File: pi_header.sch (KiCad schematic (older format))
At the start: 1 part

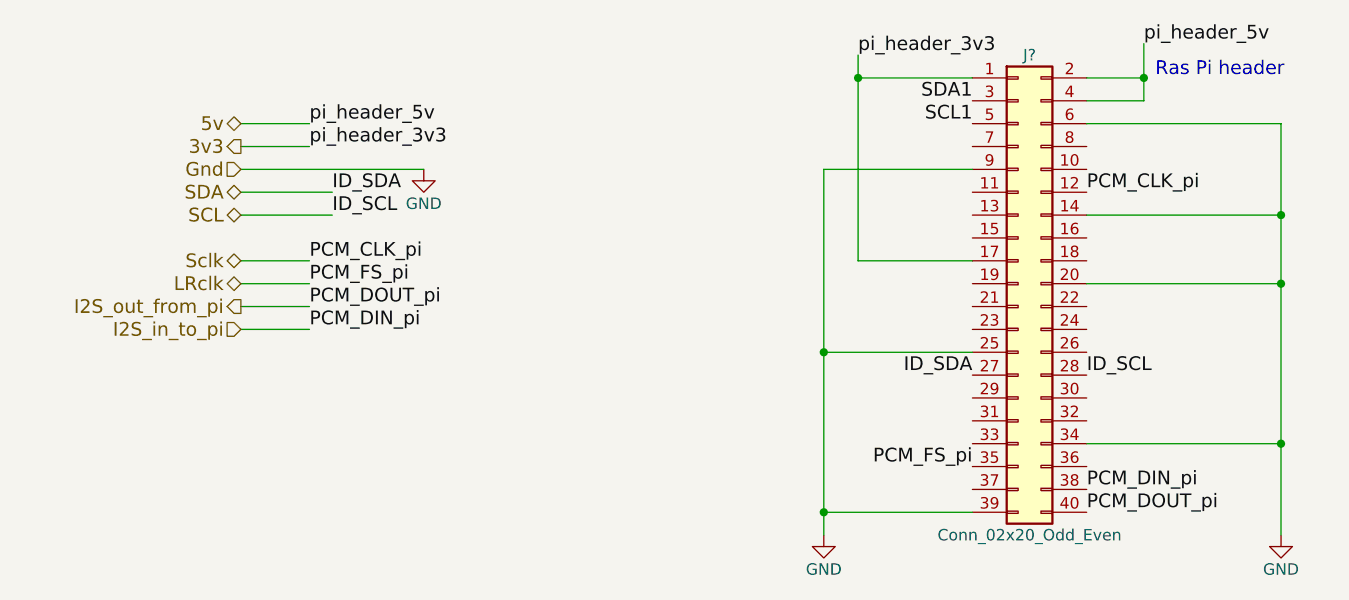
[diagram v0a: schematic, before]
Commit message: preliminary schematic using discrete logic chips
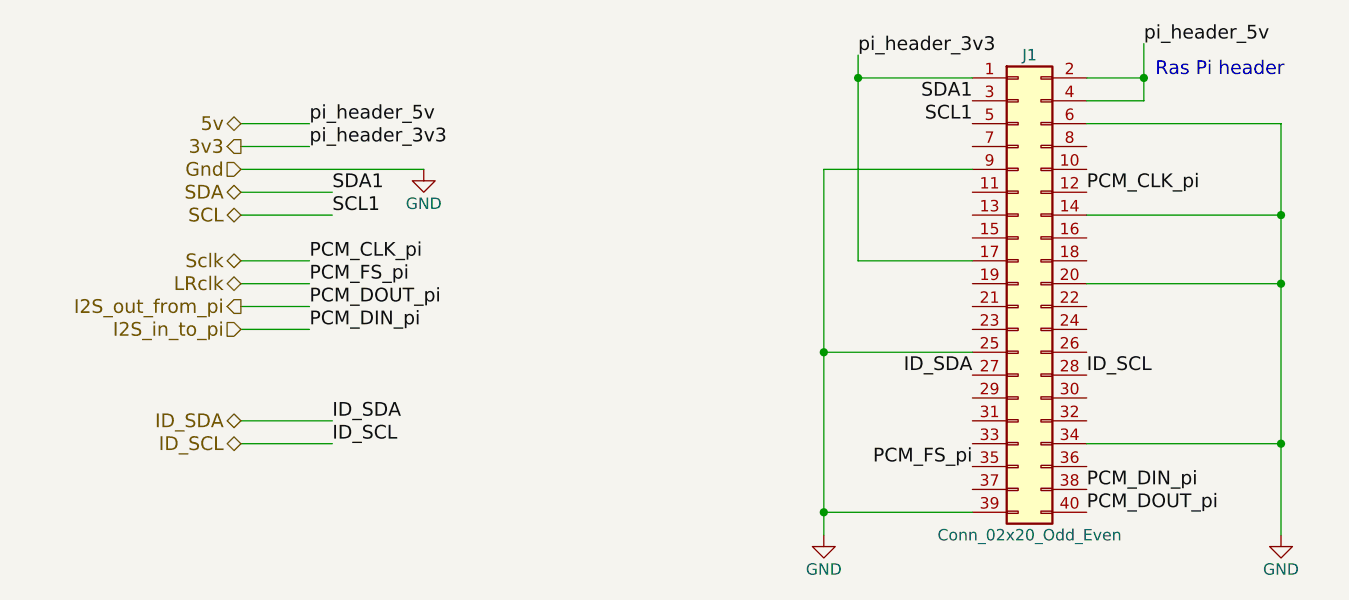
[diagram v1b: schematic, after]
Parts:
- J1: renamed from J?; footprint (none) -> Pin_Headers:Pin_Header_Straight_2x20_Pitch2.54mm
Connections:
- net SCL1 is gone; now on net SCL: J1.5 (Pin_5)
- net SDA1 is gone; now on net SDA: J1.3 (Pin_3)
- net SCL: no longer J1.28 (Pin_28)
- net SDA: no longer J1.27 (Pin_27)
- new net ID_SCL: J1.28 (Pin_28)
- new net ID_SDA: J1.27 (Pin_27)
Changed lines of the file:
@@
 LIBS:contrib
 LIBS:valves
+LIBS:74cbtlv3245
+LIBS:abb
+LIBS:tca9546a
 LIBS:flexibleaudiohub-cache
 EELAYER 25 0
@@
 $Descr A4 11693 8268
 encoding utf-8
-Sheet 2 9
+Sheet 2 10
 Title ""
 Date ""
@@
 Ras Pi header
 Wire Wire Line
-	4000 1800 4000 1900
-Wire Wire Line
-	4000 1900 4000 2700
+	4000 1800 4000 2700
 Wire Wire Line
 	4000 1900 4500 1900
@@
 Connection ~ 4000 1900
 $Comp
-L GND #PWR013
+L GND #PWR023
 U 1 1 58D8CF97
 P 3850 3900
-F 0 "#PWR013" H 3850 3650 50  0001 C CNN
+F 0 "#PWR023" H 3850 3650 50  0001 C CNN
 F 1 "GND" H 3850 3750 50  0000 C CNN
 F 2 "" H 3850 3900 50  0000 C CNN
@@
 	3850 3800 4500 3800
 Wire Wire Line
-	3850 2300 3850 3100
-Wire Wire Line
-	3850 3100 3850 3800
-Wire Wire Line
-	3850 3800 3850 3900
+	3850 2300 3850 3900
 Wire Wire Line
 	4500 3100 3850 3100
@@
 	5000 1900 5250 1900
 Wire Wire Line
-	5250 1750 5250 1900
-Wire Wire Line
-	5250 1900 5250 2000
+	5250 1750 5250 2000
 Wire Wire Line
 	5250 2000 5000 2000
 Connection ~ 5250 1900
 $Comp
-L GND #PWR015
+L GND #PWR024
 U 1 1 58D8CFAF
 P 5850 3900
-F 0 "#PWR015" H 5850 3650 50  0001 C CNN
+F 0 "#PWR024" H 5850 3650 50  0001 C CNN
 F 1 "GND" H 5850 3750 50  0000 C CNN
 F 2 "" H 5850 3900 50  0000 C CNN
@@
 	5850 3500 5000 3500
 Wire Wire Line
-	5850 2100 5850 2500
-Wire Wire Line
-	5850 2500 5850 2800
-Wire Wire Line
-	5850 2800 5850 3500
-Wire Wire Line
-	5850 3500 5850 3900
+	5850 2100 5850 3900
 Wire Wire Line
 	5000 2800 5850 2800
@@
 PCM_DOUT_pi
 $Comp
-L GND #PWR018
+L GND #PWR025
 U 1 1 58D8D147
 P 2100 2300
-F 0 "#PWR018" H 2100 2050 50  0001 C CNN
+F 0 "#PWR025" H 2100 2050 50  0001 C CNN
 F 1 "GND" H 2100 2150 50  0000 C CNN
 F 2 "" H 2100 2300 50  0000 C CNN
@@
 	1300 3000 1600 3000
 $Comp
-L Conn_02x20_Odd_Even J?
+L Conn_02x20_Odd_Even J1
 U 1 1 5AD71FB3
 P 4700 2800
-F 0 "J?" H 4750 3800 50  0000 C CNN
+F 0 "J1" H 4750 3800 50  0000 C CNN
 F 1 "Conn_02x20_Odd_Even" H 4750 1700 50  0000 C CNN
-F 2 "" H 4700 2800 50  0001 C CNN
+F 2 "Pin_Headers:Pin_Header_Straight_2x20_Pitch2.54mm" H 4700 2800 50  0001 C CNN
 F 3 "" H 4700 2800 50  0001 C CNN
 	1    4700 2800
@@
 $EndComp
 Text Label 1700 2400 0    60   ~ 0
-ID_SDA
+SDA1
 Text Label 1700 2500 0    60   ~ 0
-ID_SCL
+SCL1
 Text Label 4000 1800 0    60   ~ 0
 pi_header_3v3
@@
 Text Label 1600 2200 0    60   ~ 0
 pi_header_3v3
+Text HLabel 1300 3400 0    60   BiDi ~ 0
+ID_SDA
+Text HLabel 1300 3500 0    60   BiDi ~ 0
+ID_SCL
+Wire Wire Line
+	1300 3400 1700 3400
+Wire Wire Line
+	1300 3500 1700 3500
+Text Label 1700 3400 0    60   ~ 0
+ID_SDA
+Text Label 1700 3500 0    60   ~ 0
+ID_SCL
 $EndSCHEMATC
